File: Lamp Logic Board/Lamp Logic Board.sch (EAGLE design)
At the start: 41 parts, among them U1 ESP32-WROVER-IB, U2 SN74HCT245DWR, U3 LM1117MP-1.8, U4 PEC11S-929K-S0015, U5 WS2813, U6 MSGEQ7DIL

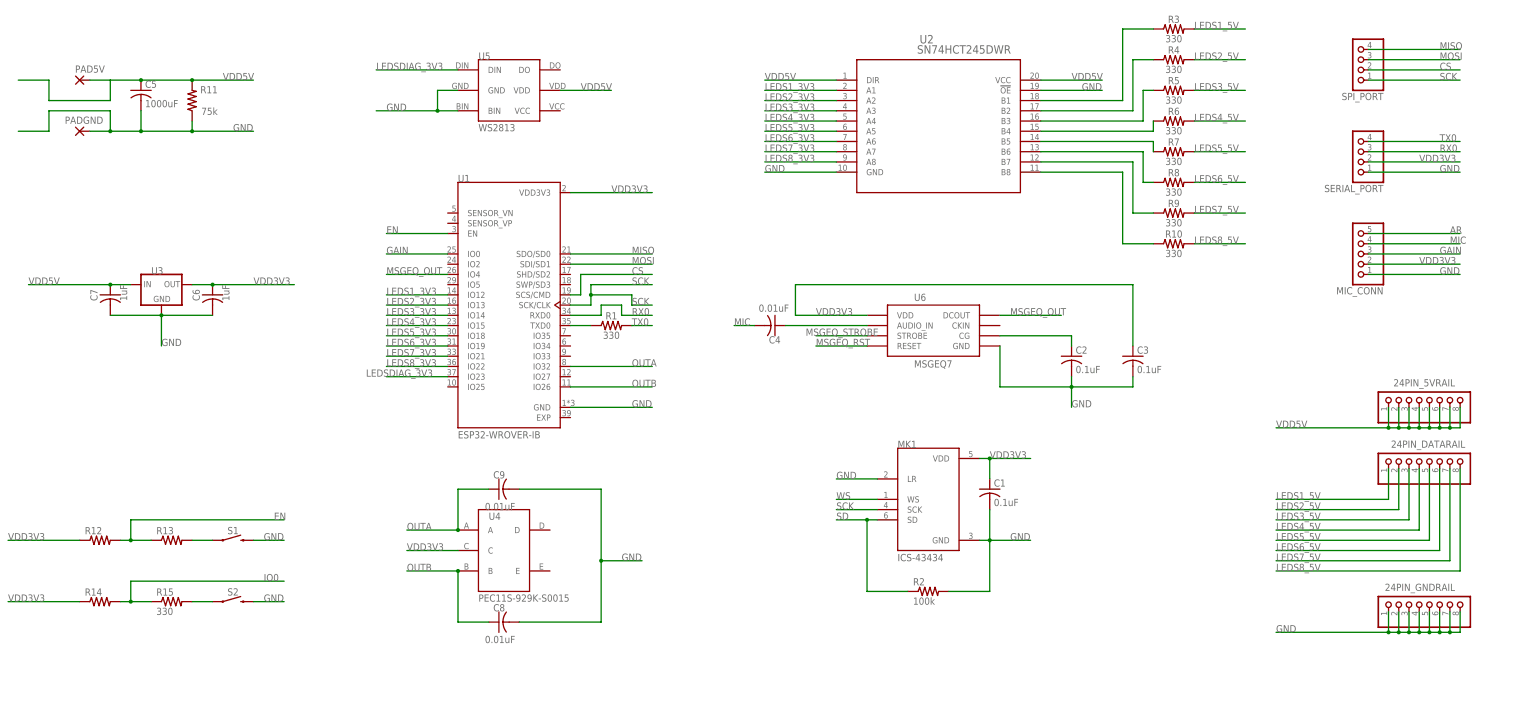
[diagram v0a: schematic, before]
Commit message: Add files via upload
First full schematic for the board, as well a components list.
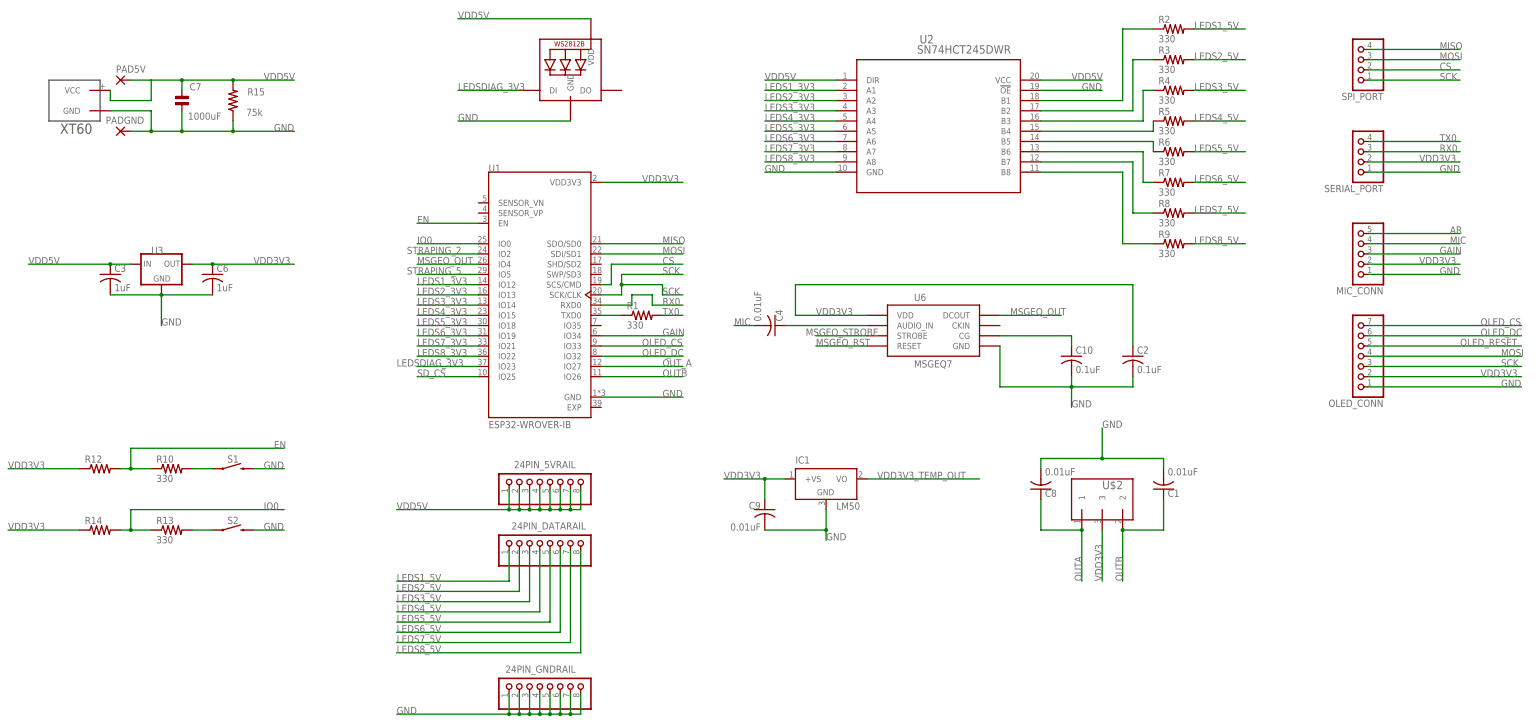
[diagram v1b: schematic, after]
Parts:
- removed C5: 1000uF, resistor:C-US050-050X075
- removed MK1: ICS-43434, ICS-43434:ICS-43434
- removed R11: 75k, resistor:R-US_0207/10
- removed U4: PEC11S-929K-S0015, PEC11S-929K-S0015 :PEC11S-929K-S0015
- removed U5: WS2813, Personal:WS2813
- added C10: 0.1uF, resistor:C-USC0805
- added IC1: LM50, linear:LM50
- added LED1: WS2812B5050, WS2812B:WS2812B5050
- added OLED_CONN: (no value), pinhead:PINHD-1X7
- added U$1: XT60, XT60:XT60
- added U$2: EN11-HSM1AF15, untitled:EN11-HSM1AF15
- C1: value 0.1uF -> 0.01uF; device resistor:C-USC1808 -> resistor:C-USC0402; SPICEPREFIX C -> (none)
- C2: device resistor:C-USC1808 -> resistor:C-USC0805; SPICEPREFIX C -> (none)
- C3: value 0.1uF -> 1uF; device resistor:C-USC1808 -> resistor:C-USC0402; SPICEPREFIX C -> (none)
- C4, C6, C8, C9: device resistor:C-USC1808 -> resistor:C-USC0402; SPICEPREFIX C -> (none)
- C7: value 1uF -> 1000uF; device resistor:C-USC1808 -> cap-pan40:C-BP-2,0X5; SPICEPREFIX C -> (none)
- R1, R10, R3, R4, R5, R6, R7, R8, R9: device SparkFun-Resistors:330OHM-0603-1/10W-1% -> resistor:R-US_R1206
- R13: value (none) -> 330; device resistor:R-US_R0603 -> resistor:R-US_R1206
- R15: value 330 -> 75k; device resistor:R-US_R0603 -> resistor:R-US_0309/12
- R2: value 100k -> 330; device resistor:R-US_R0805 -> resistor:R-US_R1206; SPICEPREFIX R -> (none)
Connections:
- removed net SD: MK1.SD, R2.1
- removed net WS: MK1.WS
- new net OLED_CS: OLED_CONN.7, U1.IO33
- new net OLED_DC: OLED_CONN.6, U1.IO32
- new net OLED_RESET: OLED_CONN.5
- new net OUT_A: U1.IO27
- new net SD_CS: U1.IO25
- new net STRAPING_2: U1.IO2
- new net STRAPING_5: U1.IO5
- new net VDD3V3_TEMP_OUT: IC1.VO
- net EN: now also R10.1; no longer R13.1
- net GAIN: now also U1.IO34; no longer U1.IO0
- net GND: now also C10.2, C7.1, IC1.GND, LED1.GND, OLED_CONN.1, R15.1, U$1.GND; no longer C5.2, C7.2, MK1.GND, MK1.LR, R11.1, R2.2, U5.BIN, U5.GND
- net IO0: now also R13.1, U1.IO0; no longer R15.1
- net LEDS1_5V: now also R2.2; no longer R3.2
- net LEDS2_5V: now also R3.2; no longer R4.2
- net LEDS3_5V: now also R4.2; no longer R5.2
- net LEDS4_5V: now also R5.2; no longer R6.2
- net LEDS5_5V: now also R6.2; no longer R7.2
- net LEDS6_5V: now also R7.2; no longer R8.2
- net LEDS7_5V: now also R8.2; no longer R9.2
- net LEDS8_5V: now also R9.2; no longer R10.2
- net LEDSDIAG_3V3: now also LED1.DI; no longer U5.DIN
- net MOSI: now also OLED_CONN.4
- net N$15: now also R2.1; no longer R3.1
- net N$16: now also R3.1; no longer R4.1
- net N$17: now also R4.1; no longer R5.1
- net N$18: now also R5.1; no longer R6.1
- net N$19: now also R6.1; no longer R7.1
- net N$20: now also R7.1; no longer R8.1
- net N$21: now also R8.1; no longer R9.1
- net N$22: now also R9.1; no longer R10.1
- net N$4: now also C10.1; no longer C2.1
- net N$7: now also R13.2; no longer R15.2
- net N$9: now also R10.2; no longer R13.2
- net OUTA: now also C8.1, U$2.1; no longer C9.1, U1.IO32, U4.A
- net OUTB: now also C1.1, U$2.2; no longer C8.1, U4.B
- net SCK: now also OLED_CONN.3; no longer MK1.SCK
- net VDD3V3: now also C2.1, C9.1, IC1.+VS, OLED_CONN.2, U$2.3; no longer C1.1, C3.1, MK1.VDD, U4.C
- net VDD5V: now also C3.1, C7.2, LED1.VDD, R15.2, U$1.VCC; no longer C5.1, C7.1, R11.2, U5.VDD
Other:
- moved on the sheet: 24PIN_5VRAIL, 24PIN_DATARAIL, 24PIN_GNDRAIL, C1, C2, C3, C6, C8, C9, PAD5V, PADGND, R1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

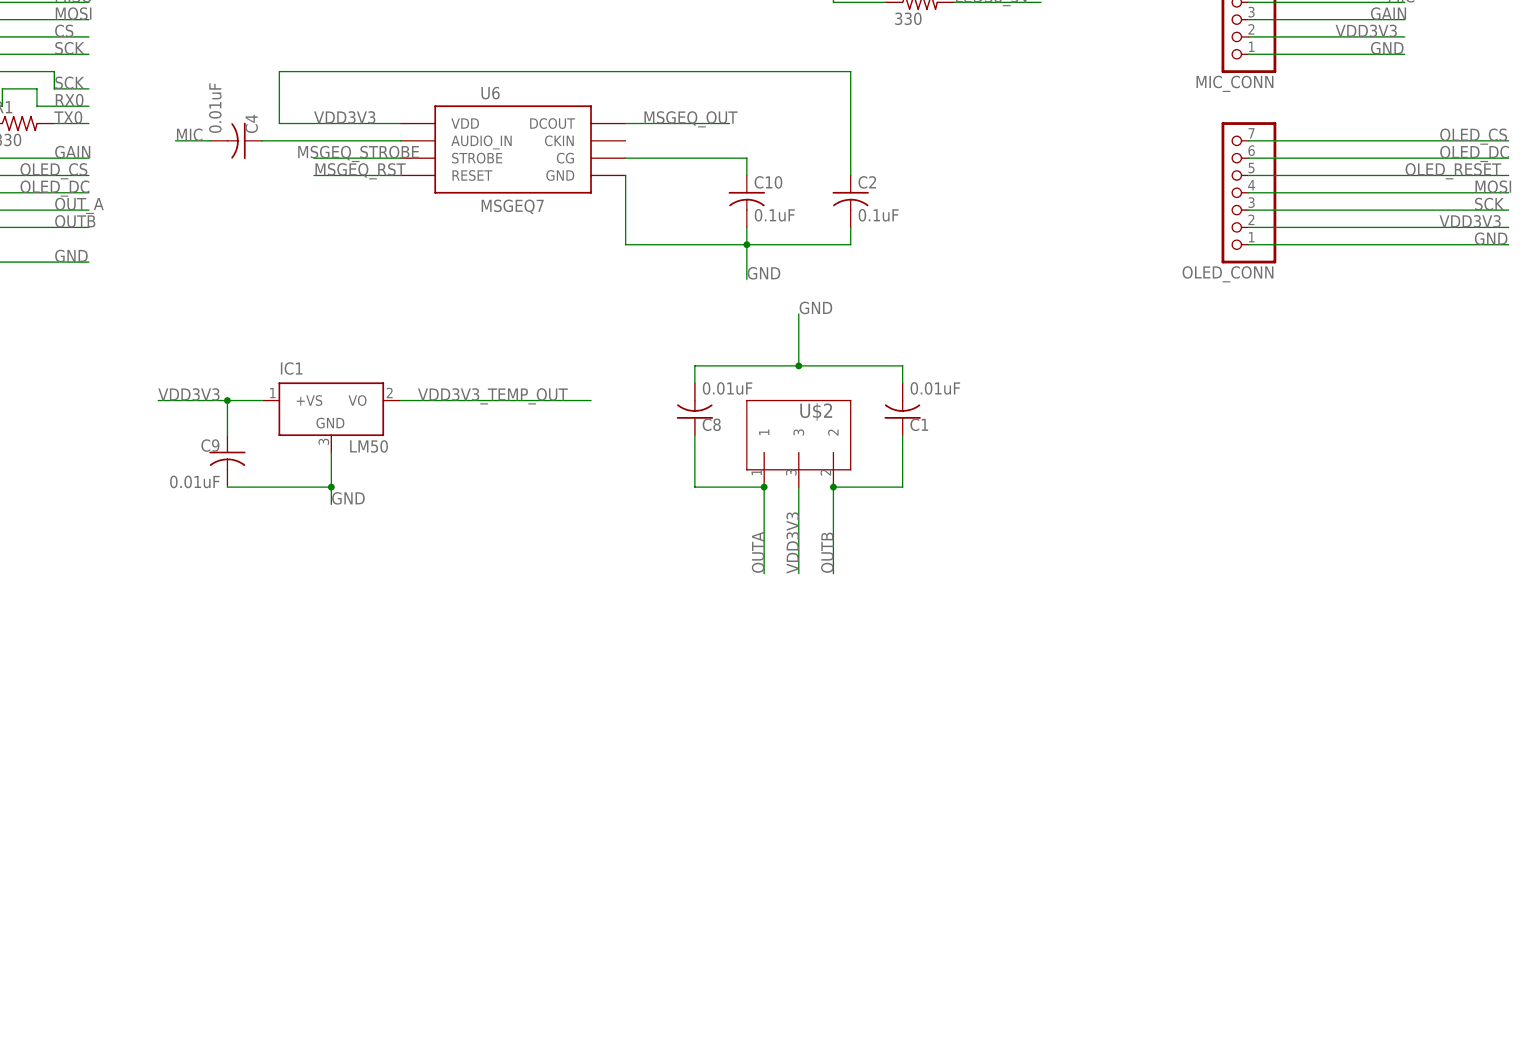
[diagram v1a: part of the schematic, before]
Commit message: Add files via upload
Added the SD Card Connector as well ESD Filter for it.
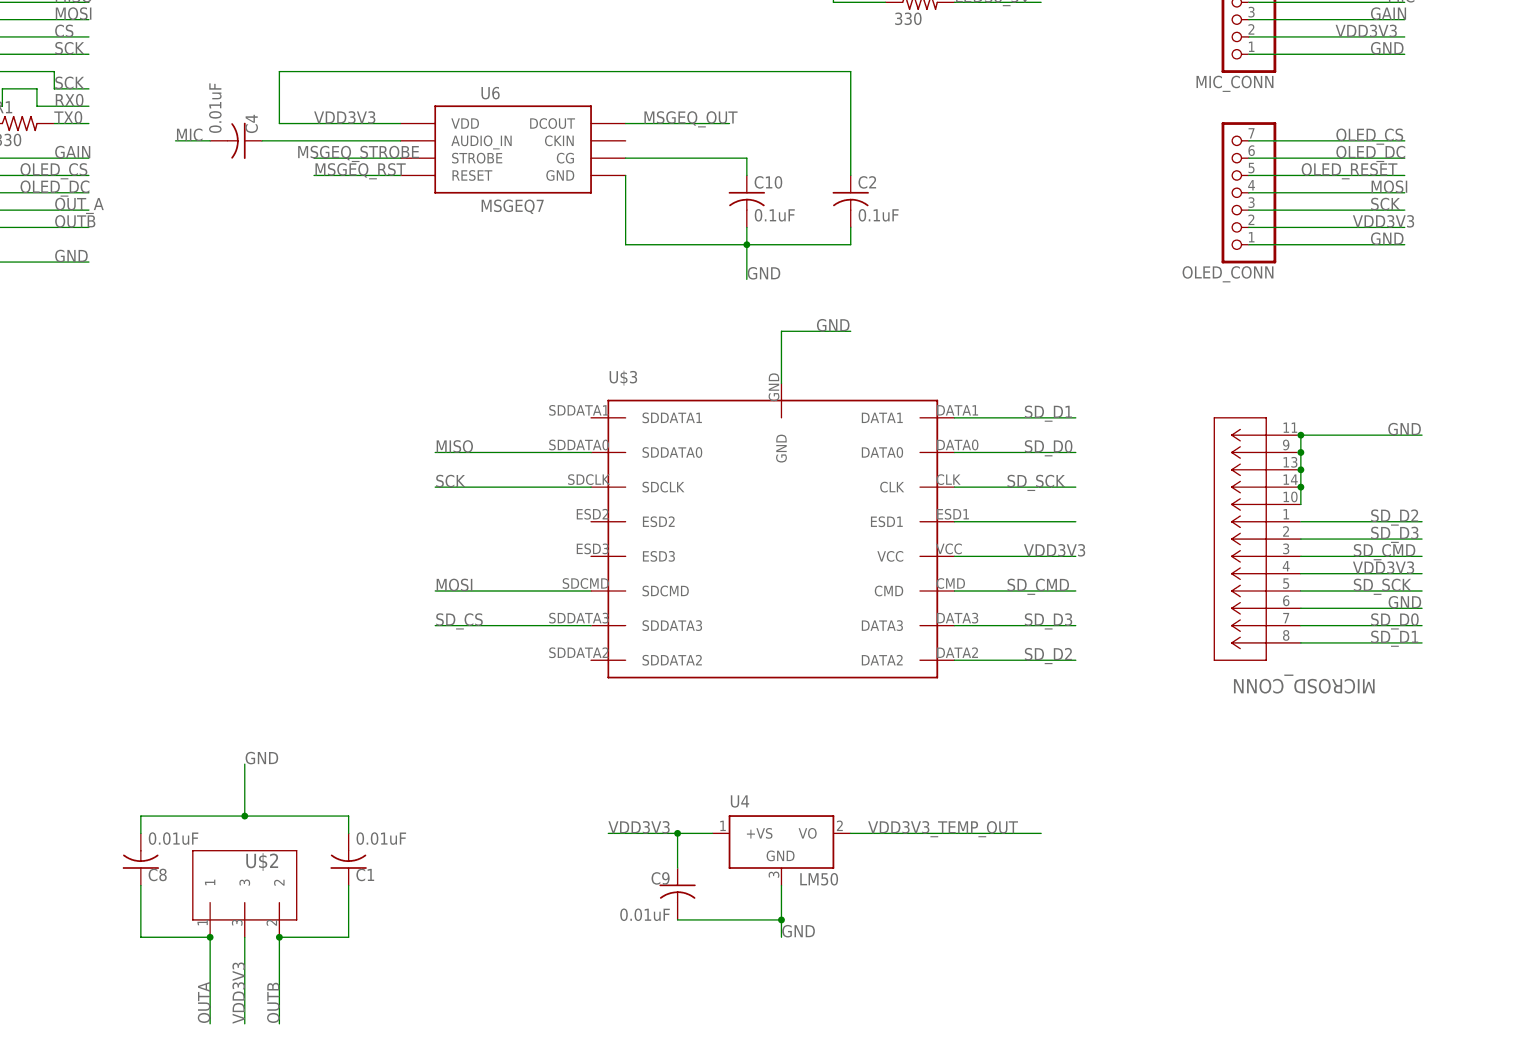
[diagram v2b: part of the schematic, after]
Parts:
- removed IC1: LM50, linear:LM50
- added MICROSD_CONN: LLC, 5027740891:LLC
- added U$3: CM1624-08DE, CM1624-08DE:CM1624-08DE
- added U4: LM50, linear:LM50
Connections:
- new net N$8: U$3.ESD1
- new net SD_CMD: MICROSD_CONN.3, U$3.CMD
- new net SD_D0: MICROSD_CONN.7, U$3.DATA0
- new net SD_D1: MICROSD_CONN.8, U$3.DATA1
- new net SD_D2: MICROSD_CONN.1, U$3.DATA2
- new net SD_D3: MICROSD_CONN.2, U$3.DATA3
- new net SD_SCK: MICROSD_CONN.5, U$3.CLK
- net GND: now also MICROSD_CONN.10, MICROSD_CONN.11, MICROSD_CONN.13, MICROSD_CONN.14, MICROSD_CONN.6, MICROSD_CONN.9, U$3.GND, U4.GND; no longer IC1.GND
- net MISO: now also U$3.SDDATA0
- net MOSI: now also U$3.SDCMD
- net SCK: now also U$3.SDCLK
- net SD_CS: now also U$3.SDDATA3
- net VDD3V3: now also MICROSD_CONN.4, U$3.VCC, U4.+VS; no longer IC1.+VS
- net VDD3V3_TEMP_OUT: now also U4.VO; no longer IC1.VO
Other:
- moved on the sheet: C1, C8, C9, U$2
